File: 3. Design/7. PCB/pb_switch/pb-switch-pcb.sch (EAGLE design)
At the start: 8 parts, among them Q1 2N7002NXAKR

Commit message: ADD|UPDT: PB switch PCB 3D model
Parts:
- removed S1: DTS-6, switch-tact:DTS-6
- added C1: 100n [0603], Capacitor:C_CHIP-0603(1608-METRIC)
- added SW1: B3F-1000, Switch:B3F-1000
- R2: value 100k [0603] -> 1M [0603]
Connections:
- net GND: now also C1.2, SW1.1; no longer S1.2
- net N$2: now also SW1.3; no longer S1.4
- net VOUT: now also C1.1
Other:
- moved on the sheet: R2
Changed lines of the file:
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@@
 <layer number="133" name="bottom_silk" color="7" fill="1" visible="yes" active="yes"/>
 <layer number="144" name="Drill_legend" color="7" fill="1" visible="yes" active="yes"/>
+<layer number="145" name="DrillLegend_01-16" color="2" fill="9" visible="no" active="yes"/>
+<layer number="146" name="DrillLegend_01-20" color="3" fill="9" visible="no" active="yes"/>
 <layer number="150" name="Notes" color="7" fill="1" visible="yes" active="yes"/>
 <layer number="151" name="HeatSink" color="7" fill="1" visible="yes" active="yes"/>
@@
 </classes>
 <parts>
-<part name="PB_CTRL" library="MAX16150AUT+T" deviceset="MAX16150AUT+T" device=""/>
-<part name="Q1" library="2N7002NXAKR" deviceset="2N7002NXAKR" device=""/>
+<part name="PB_CTRL" library="MAX16150AUT+T" deviceset="MAX16150AUT+T" device="" override_package3d_urn="urn:adsk.eagle:package:25385618/2" override_package_urn="urn:adsk.eagle:footprint:25385620/1"/>
+<part name="Q1" library="2N7002NXAKR" deviceset="2N7002NXAKR" device="" override_package3d_urn="urn:adsk.eagle:package:25385597/2" override_package_urn="urn:adsk.eagle:footprint:25385598/1"/>
 <part name="GND2" library="SparkFun-PowerSymbols" library_urn="urn:adsk.eagle:library:530" deviceset="GND" device=""/>
 <part name="R1" library="Resistor" library_urn="urn:adsk.eagle:library:16378527" deviceset="R-US" device="CHIP-0603(1608-METRIC)" package3d_urn="urn:adsk.eagle:package:16378565/2" technology="_" value="1.4K[0603]"/>
 <part name="R5" library="Resistor" library_urn="urn:adsk.eagle:library:16378527" deviceset="R-US" device="CHIP-0603(1608-METRIC)" package3d_urn="urn:adsk.eagle:package:16378565/2" technology="_" value="1.4K[0603]"/>
 <part name="R6" library="Resistor" library_urn="urn:adsk.eagle:library:16378527" deviceset="R-US" device="CHIP-0603(1608-METRIC)" package3d_urn="urn:adsk.eagle:package:16378565/2" technology="_" value="1.4K[0603]"/>
-<part name="R2" library="Resistor" library_urn="urn:adsk.eagle:library:16378527" deviceset="R-US" device="CHIP-0603(1608-METRIC)" package3d_urn="urn:adsk.eagle:package:16378565/2" technology="_" value="100k [0603]"/>
-<part name="S1" library="switch-tact" deviceset="DTS-6" device=""/>
 <part name="J1" library="SparkFun-Connectors" library_urn="urn:adsk.eagle:library:513" deviceset="CONN_05" device="" package3d_urn="urn:adsk.eagle:package:38104/1"/>
-<part name="GND1" library="SparkFun-PowerSymbols" library_urn="urn:adsk.eagle:library:530" deviceset="GND" device=""/>
 <part name="GND3" library="SparkFun-PowerSymbols" library_urn="urn:adsk.eagle:library:530" deviceset="GND" device=""/>
+<part name="SW1" library="Switch" library_urn="urn:adsk.eagle:library:11396471" deviceset="B3F-1000" device="" package3d_urn="urn:adsk.eagle:package:10899221/2"/>
+<part name="C1" library="Capacitor" library_urn="urn:adsk.eagle:library:16290819" deviceset="C" device="CHIP-0603(1608-METRIC)" package3d_urn="urn:adsk.eagle:package:16290898/2" technology="_" value="100n [0603]"/>
+<part name="GND4" library="SparkFun-PowerSymbols" library_urn="urn:adsk.eagle:library:530" deviceset="GND" device=""/>
+<part name="R2" library="Resistor" library_urn="urn:adsk.eagle:library:16378527" deviceset="R-US" device="CHIP-0603(1608-METRIC)" package3d_urn="urn:adsk.eagle:package:16378565/2" technology="_" value="1M [0603]"/>
 </parts>
 <sheets>
@@
 <attribute name="VALUE" x="-29.718" y="68.58" size="1.778" layer="96" rot="R90" align="center"/>
 </instance>
-<instance part="R2" gate="G$1" x="-6.35" y="39.37" smashed="yes" rot="R90">
-<attribute name="NAME" x="-7.8486" y="39.37" size="1.778" layer="95" rot="R90" align="center"/>
-<attribute name="VALUE" x="-4.318" y="38.1" size="1.778" layer="96" rot="R90" align="center"/>
-</instance>
-<instance part="S1" gate="G$1" x="-92.71" y="58.42" smashed="yes">
-<attribute name="NAME" x="-99.06" y="55.88" size="1.778" layer="95" rot="R90"/>
-<attribute name="VALUE" x="-96.52" y="61.595" size="1.778" layer="96" rot="R90"/>
-</instance>
 <instance part="J1" gate="G$1" x="-52.07" y="33.02" smashed="yes">
 <attribute name="VALUE" x="-54.61" y="23.114" size="1.778" layer="96" font="vector"/>
 <attribute name="NAME" x="-54.61" y="41.148" size="1.778" layer="95" font="vector"/>
 </instance>
-<instance part="GND1" gate="1" x="-6.35" y="31.75" smashed="yes">
-<attribute name="VALUE" x="-6.35" y="30.226" size="1.778" layer="96" align="top-center"/>
-</instance>
 <instance part="GND3" gate="1" x="-44.45" y="25.4" smashed="yes">
 <attribute name="VALUE" x="-44.45" y="23.876" size="1.778" layer="96" align="top-center"/>
+</instance>
+<instance part="SW1" gate="G$1" x="-101.6" y="59.69" smashed="yes">
+<attribute name="NAME" x="-109.226109375" y="68.078109375" size="1.27101875" layer="95"/>
+<attribute name="VALUE" x="-109.231590625" y="50.02448125" size="1.27193125" layer="96"/>
+</instance>
+<instance part="C1" gate="G$1" x="1.27" y="44.45" smashed="yes">
+<attribute name="NAME" x="3.81" y="43.18" size="1.778" layer="95"/>
+<attribute name="VALUE" x="3.81" y="40.64" size="1.778" layer="96"/>
+</instance>
+<instance part="GND4" gate="1" x="1.27" y="34.29" smashed="yes">
+<attribute name="VALUE" x="1.27" y="32.766" size="1.778" layer="96" align="top-center"/>
+</instance>
+<instance part="R2" gate="G$1" x="-6.35" y="43.18" smashed="yes" rot="R90">
+<attribute name="NAME" x="-7.8486" y="43.18" size="1.778" layer="95" rot="R90" align="center"/>
+<attribute name="VALUE" x="-4.318" y="41.91" size="1.778" layer="96" rot="R90" align="center"/>
 </instance>
 </instances>
@@
 <wire x1="-83.82" y1="53.34" x2="-83.82" y2="52.07" width="0.1524" layer="91"/>
 <wire x1="-71.12" y1="57.15" x2="-83.82" y2="57.15" width="0.1524" layer="91"/>
-<pinref part="S1" gate="G$1" pin="2"/>
 <wire x1="-90.17" y1="53.34" x2="-83.82" y2="53.34" width="0.1524" layer="91"/>
 <junction x="-83.82" y="53.34"/>
-</segment>
-<segment>
-<pinref part="GND1" gate="1" pin="GND"/>
-<pinref part="R2" gate="G$1" pin="1"/>
+<pinref part="SW1" gate="G$1" pin="1"/>
+<wire x1="-90.17" y1="53.34" x2="-90.17" y2="54.61" width="0.1524" layer="91"/>
+<wire x1="-90.17" y1="54.61" x2="-91.44" y2="54.61" width="0.1524" layer="91"/>
 </segment>
 <segment>
@@
 <junction x="-44.45" y="27.94"/>
 </segment>
+<segment>
+<pinref part="GND4" gate="1" pin="GND"/>
+<pinref part="C1" gate="G$1" pin="2"/>
+<wire x1="1.27" y1="36.83" x2="1.27" y2="39.37" width="0.1524" layer="91"/>
+<pinref part="R2" gate="G$1" pin="1"/>
+<wire x1="-6.35" y1="38.1" x2="-6.35" y2="36.83" width="0.1524" layer="91"/>
+<wire x1="-6.35" y1="36.83" x2="1.27" y2="36.83" width="0.1524" layer="91"/>
+<junction x="1.27" y="36.83"/>
+</segment>
 </net>
 <net name="N$2" class="0">
@@
 <wire x1="-83.82" y1="59.69" x2="-71.12" y2="59.69" width="0.1524" layer="91"/>
 <pinref part="R1" gate="G$1" pin="1"/>
-<pinref part="S1" gate="G$1" pin="4"/>
 <wire x1="-90.17" y1="63.5" x2="-83.82" y2="63.5" width="0.1524" layer="91"/>
 <junction x="-83.82" y="63.5"/>
+<wire x1="-90.17" y1="63.5" x2="-90.17" y2="62.23" width="0.1524" layer="91"/>
+<pinref part="SW1" gate="G$1" pin="3"/>
+<wire x1="-90.17" y1="62.23" x2="-91.44" y2="62.23" width="0.1524" layer="91"/>
 </segment>
 </net>
@@
 <net name="VOUT" class="0">
 <segment>
-<pinref part="Q1" gate="G$1" pin="S"/>
-<wire x1="-6.35" y1="49.53" x2="-6.35" y2="48.26" width="0.1524" layer="91"/>
-<label x="-6.35" y="46.99" size="1.778" layer="95" xref="yes"/>
-<pinref part="R2" gate="G$1" pin="2"/>
-<wire x1="-6.35" y1="48.26" x2="-6.35" y2="46.99" width="0.1524" layer="91"/>
-<wire x1="-6.35" y1="46.99" x2="-6.35" y2="44.45" width="0.1524" layer="91"/>
-</segment>
-<segment>
 <pinref part="J1" gate="G$1" pin="3"/>
 <pinref part="J1" gate="G$1" pin="4"/>
 <wire x1="-44.45" y1="33.02" x2="-44.45" y2="35.56" width="0.1524" layer="91"/>
 <label x="-44.45" y="34.29" size="1.778" layer="95" xref="yes"/>
+</segment>
+<segment>
+<pinref part="R2" gate="G$1" pin="2"/>
+<wire x1="-6.35" y1="49.53" x2="-6.35" y2="48.26" width="0.1524" layer="91"/>
+<pinref part="C1" gate="G$1" pin="1"/>
+<wire x1="1.27" y1="46.99" x2="1.27" y2="49.53" width="0.1524" layer="91"/>
+<label x="1.27" y="49.53" size="1.778" layer="95" xref="yes"/>
+<wire x1="-6.35" y1="49.53" x2="1.27" y2="49.53" width="0.1524" layer="91"/>
+<pinref part="Q1" gate="G$1" pin="S"/>
+<junction x="-6.35" y="49.53"/>
 </segment>
 </net>
@@
 <segment>
 <pinref part="PB_CTRL" gate="G$1" pin="VCC"/>
+<label x="-74.93" y="54.61" size="1.778" layer="95" rot="R180" xref="yes"/>
 <wire x1="-71.12" y1="54.61" x2="-74.93" y2="54.61" width="0.1524" layer="91"/>
-<label x="-74.93" y="54.61" size="1.778" layer="95" rot="R180" xref="yes"/>
 </segment>
 </net>
@@
 packages will not be understood (or retained) with this version.
 </note>
+<note version="9.4" severity="warning">
+Since Version 9.4, EAGLE supports the overriding of 3D packages
+in schematics and board files. Those overridden 3d packages
+will not be understood (or retained) with this version.
+</note>
 <note version="8.4" severity="warning">

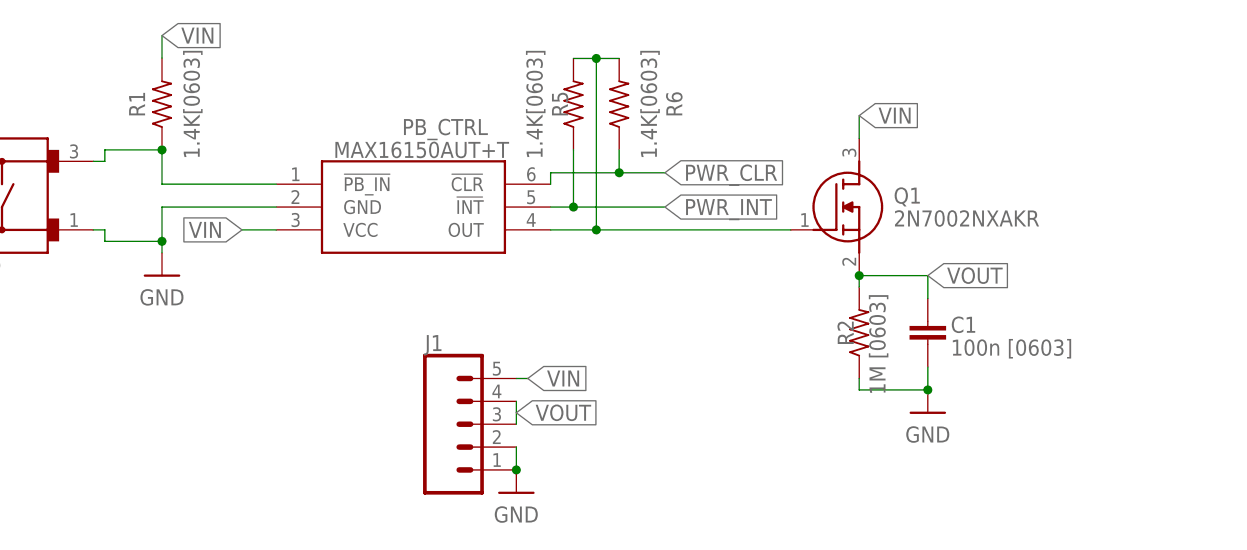
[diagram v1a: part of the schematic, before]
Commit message: FIX: replaced load switching MOSFET with an actual load switch
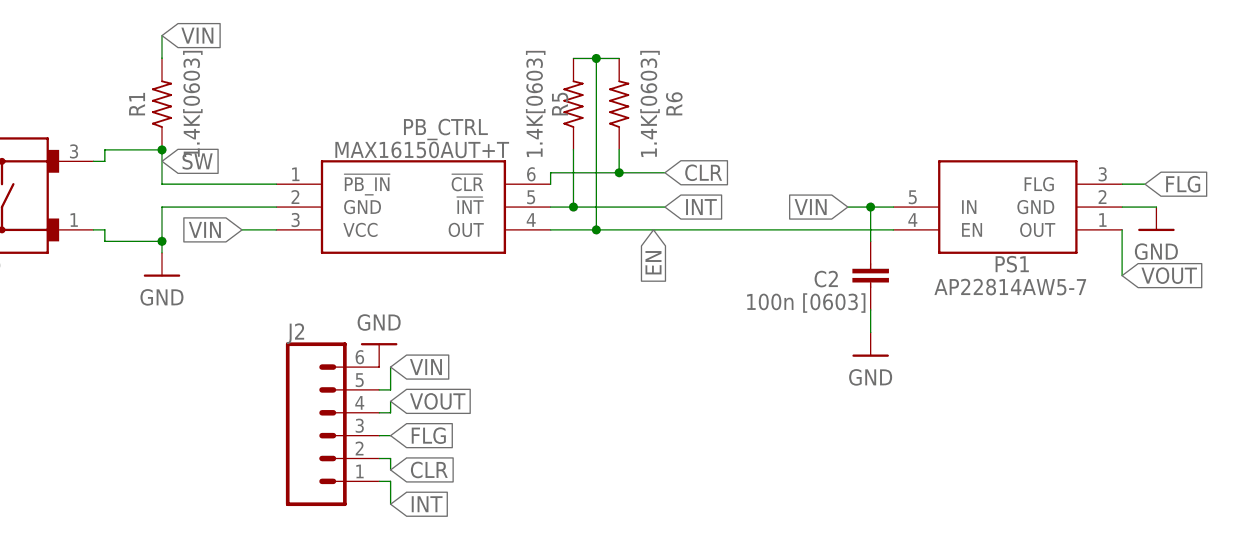
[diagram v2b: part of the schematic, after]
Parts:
- removed C1: 100n [0603], Capacitor:C_CHIP-0603(1608-METRIC)
- removed J1: (no value), SparkFun-Connectors:CONN_05
- removed Q1: 2N7002NXAKR, 2N7002NXAKR:2N7002NXAKR
- removed R2: 1M [0603], Resistor:R-US_CHIP-0603(1608-METRIC)
- added C2: 100n [0603], Capacitor:C_CHIP-0603(1608-METRIC)
- added J2: (no value), SparkFun-Connectors:CONN_06SILK_FEMALE_PTH
- added PS1: AP22814AW5-7, AP22814AW5-7:AP22814AW5-7
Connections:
- net N$2 renamed SW
- removed net N$5: PB_CTRL.OUT, Q1.G, R5.2, R6.2
- removed net PWR_CLR: PB_CTRL.!CLR, R6.1
- removed net PWR_INT: PB_CTRL.!INT, R5.1
- new net CLR: J2.2, PB_CTRL.!CLR, R6.1
- new net EN: PB_CTRL.OUT, PS1.EN, R5.2, R6.2
- new net FLG: J2.3, PS1.FLG
- new net INT: J2.1, PB_CTRL.!INT, R5.1
- net GND: now also C2.2, J2.6, PS1.GND; no longer C1.2, J1.1, J1.2, R2.1
- net VIN: now also C2.1, J2.5, PS1.IN; no longer J1.5, Q1.D
- net VOUT: now also J2.4, PS1.OUT; no longer C1.1, J1.3, J1.4, Q1.S, R2.2

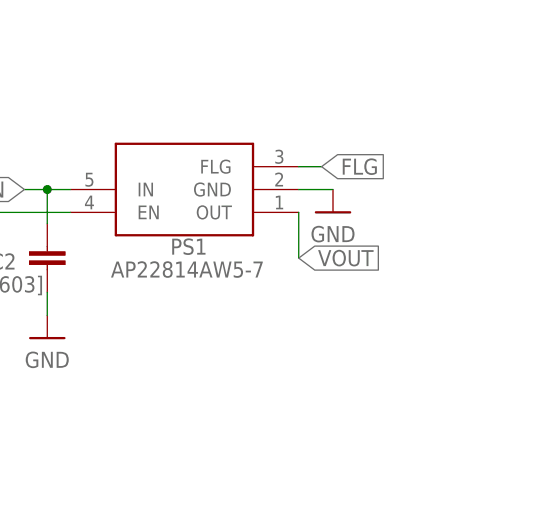
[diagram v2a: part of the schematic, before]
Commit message: UPDT: Added bypass capacitor at the output, enlarged power paths and optimized power
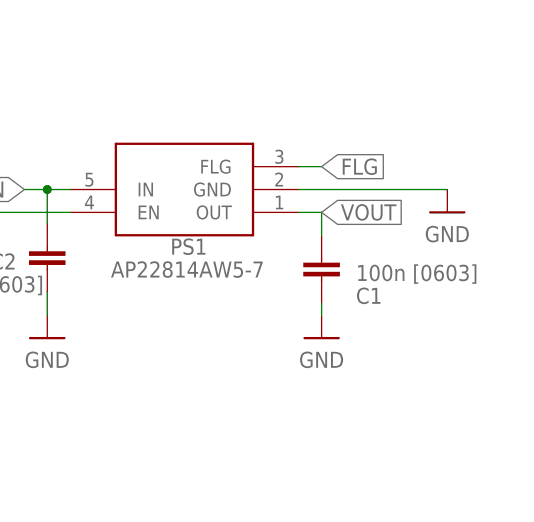
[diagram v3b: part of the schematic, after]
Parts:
- added C1: 100n [0603], Capacitor:C_CHIP-0603(1608-METRIC)
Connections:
- net GND: now also C1.2
- net VOUT: now also C1.1
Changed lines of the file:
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@@
 <part name="GND4" library="SparkFun-PowerSymbols" library_urn="urn:adsk.eagle:library:530" deviceset="GND" device=""/>
 <part name="GND3" library="SparkFun-PowerSymbols" library_urn="urn:adsk.eagle:library:530" deviceset="GND" device=""/>
+<part name="C1" library="Capacitor" library_urn="urn:adsk.eagle:library:16290819" deviceset="C" device="CHIP-0603(1608-METRIC)" package3d_urn="urn:adsk.eagle:package:16290898/2" technology="_" value="100n [0603]"/>
+<part name="GND5" library="SparkFun-PowerSymbols" library_urn="urn:adsk.eagle:library:530" deviceset="GND" device=""/>
 </parts>
 <sheets>
@@
 <attribute name="VALUE" x="19.05" y="48.26" size="1.778" layer="96" rot="R180" align="center-left"/>
 </instance>
-<instance part="GND1" gate="1" x="26.67" y="54.61" smashed="yes">
-<attribute name="VALUE" x="26.67" y="53.086" size="1.778" layer="96" align="top-center"/>
+<instance part="GND1" gate="1" x="39.37" y="54.61" smashed="yes">
+<attribute name="VALUE" x="39.37" y="53.086" size="1.778" layer="96" align="top-center"/>
 </instance>
 <instance part="J2" gate="G$1" x="-64.77" y="31.75" smashed="yes">
@@
 <instance part="GND3" gate="1" x="-59.69" y="41.91" smashed="yes" rot="R180">
 <attribute name="VALUE" x="-59.69" y="43.434" size="1.778" layer="96" rot="R180" align="top-center"/>
+</instance>
+<instance part="C1" gate="G$1" x="25.4" y="49.53" smashed="yes">
+<attribute name="NAME" x="29.21" y="44.45" size="1.778" layer="95"/>
+<attribute name="VALUE" x="29.21" y="46.99" size="1.778" layer="96"/>
+</instance>
+<instance part="GND5" gate="1" x="25.4" y="40.64" smashed="yes">
+<attribute name="VALUE" x="25.4" y="39.116" size="1.778" layer="96" align="top-center"/>
 </instance>
 </instances>
@@
 <pinref part="GND1" gate="1" pin="GND"/>
 <pinref part="PS1" gate="G$1" pin="GND"/>
-<wire x1="22.86" y1="57.15" x2="26.67" y2="57.15" width="0.1524" layer="91"/>
+<wire x1="22.86" y1="57.15" x2="39.37" y2="57.15" width="0.1524" layer="91"/>
 </segment>
 <segment>
@@
 <pinref part="GND3" gate="1" pin="GND"/>
 <pinref part="J2" gate="G$1" pin="6"/>
+</segment>
+<segment>
+<pinref part="GND5" gate="1" pin="GND"/>
+<pinref part="C1" gate="G$1" pin="2"/>
+<wire x1="25.4" y1="43.18" x2="25.4" y2="44.45" width="0.1524" layer="91"/>
 </segment>
 </net>
@@
 <net name="VOUT" class="0">
 <segment>
-<pinref part="PS1" gate="G$1" pin="OUT"/>
-<wire x1="22.86" y1="54.61" x2="22.86" y2="49.53" width="0.1524" layer="91"/>
-<label x="22.86" y="49.53" size="1.778" layer="95" xref="yes"/>
-</segment>
-<segment>
 <wire x1="-59.69" y1="34.29" x2="-58.42" y2="34.29" width="0.1524" layer="91"/>
 <label x="-58.42" y="35.56" size="1.778" layer="95" xref="yes"/>
@@
 <pinref part="J2" gate="G$1" pin="4"/>
 </segment>
+<segment>
+<pinref part="PS1" gate="G$1" pin="OUT"/>
+<pinref part="C1" gate="G$1" pin="1"/>
+<wire x1="22.86" y1="54.61" x2="25.4" y2="54.61" width="0.1524" layer="91"/>
+<wire x1="25.4" y1="54.61" x2="25.4" y2="52.07" width="0.1524" layer="91"/>
+<label x="25.4" y="54.61" size="1.778" layer="95" xref="yes"/>
+</segment>
 </net>

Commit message: ADD|UPDT: Exported new and corrected old 3D models, 2D models and technical drawings of all  PCBs
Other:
- note added: "Push Button Power Switch"
- note added: "Push Button power switch based on the MAX16150 push button switch controller and the AP22814 load switch"
- moved on the sheet: C1, C2, J2, PB_CTRL, PS1, R1, R5, R6, SW1
